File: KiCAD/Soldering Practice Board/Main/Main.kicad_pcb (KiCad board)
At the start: 2 copper layers, 7 parts, among them U1 STM32C071R8Tx, U2 BMI160, U3 LSM6DS3

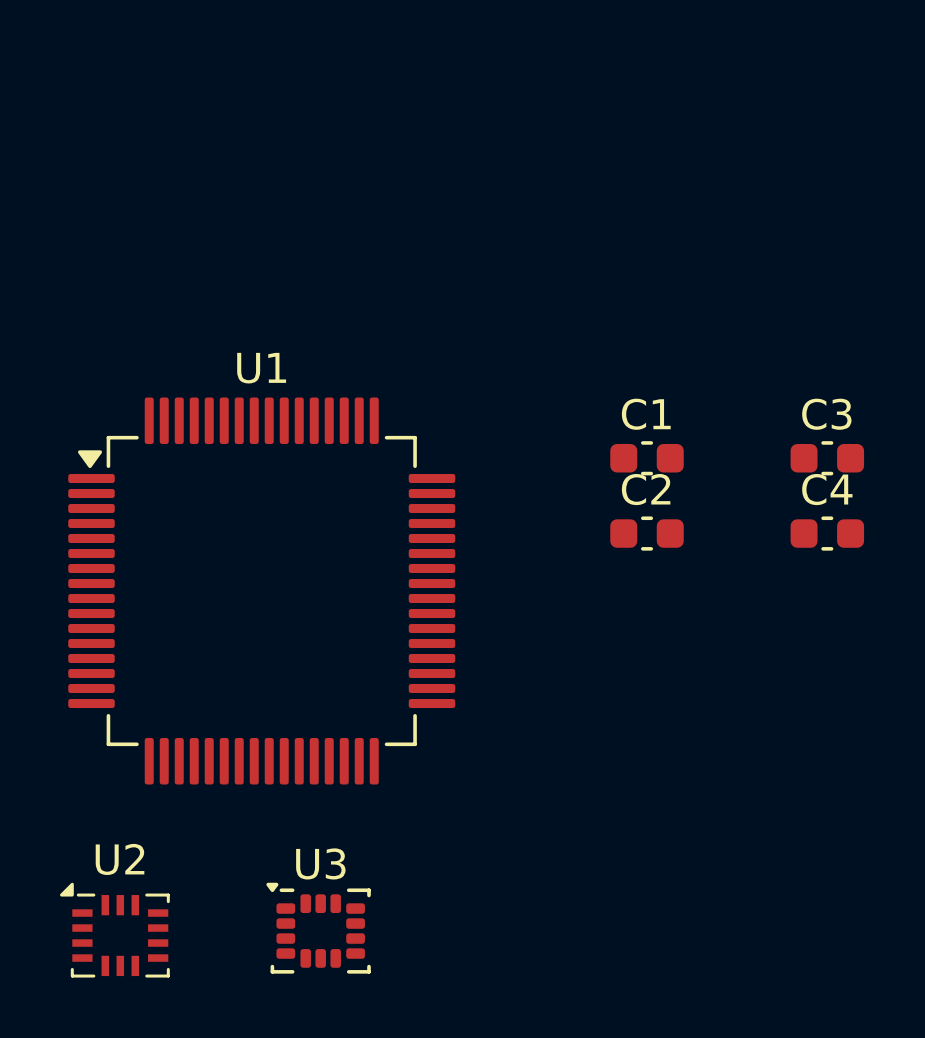
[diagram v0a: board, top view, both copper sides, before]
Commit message: Define more mcu pins
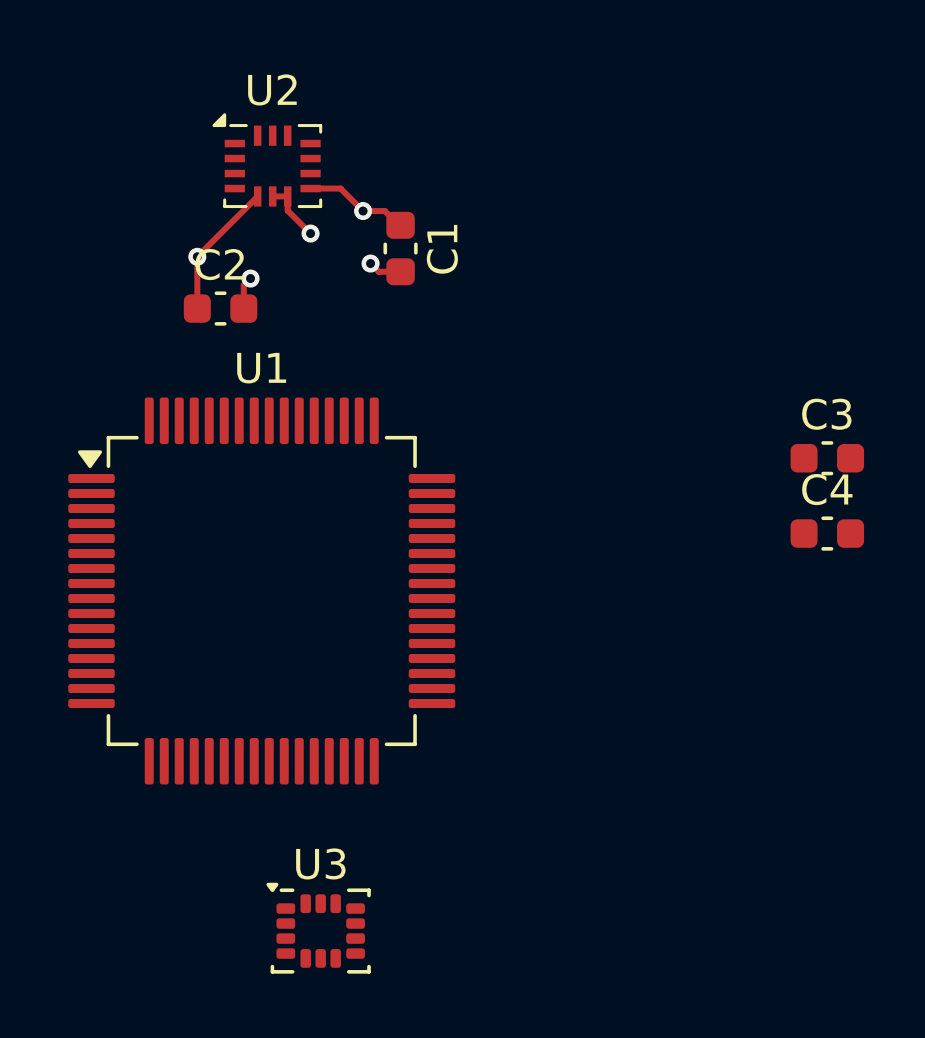
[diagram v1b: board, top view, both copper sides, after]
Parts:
- moved U2 26.1 mm to (141.7, 74.2)
- moved C2 16.1 mm to (140.0, 79.0)
- moved C1 10.8 mm to (146.0, 77.0), turned to -90 degrees
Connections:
- U1 pad 16: unconnected-(U1-PC3-Pad16) -> /TIM2_CH3
- U1 pad 25: unconnected-(U1-PC4-Pad25) -> /USART1_TX
- U1 pad 26: unconnected-(U1-PC5-Pad26) -> /USART1_RX
- U1 pad 36: unconnected-(U1-PA8-Pad36) -> /TIM1_CH1
- U1 pad 45: unconnected-(U1-PA13-Pad45) -> /SWDIO
- U1 pad 46: unconnected-(U1-PA14-Pad46) -> /SWCLK
- U1 pad 53: unconnected-(U1-PD3-Pad53) -> /STLIS_CS
- U1 pad 54: unconnected-(U1-PD4-Pad54) -> /BMI_CS
- U1 pad 55: unconnected-(U1-PD5-Pad55) -> /SPI1_MISO
- U1 pad 56: unconnected-(U1-PD6-Pad56) -> /SPI1_MOSI
- U1 pad 57: unconnected-(U1-PB3-Pad57) -> /SPI1_SCK
- U1 pad 60: unconnected-(U1-PB6-Pad60) -> /I2C1_SCL
- U1 pad 61: unconnected-(U1-PB7-Pad61) -> /I2C1_SDA
- U1 pad 7: unconnected-(U1-VREF+-Pad7) -> +3V3
- U1 pad 8: unconnected-(U1-VDD-Pad8) -> +3V3
- U1 pad 9: unconnected-(U1-VSS-Pad9) -> GND
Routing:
- net +3V3: track 0.00 -> 7.71 mm, vias 0 -> 2
- net GND: track 0.00 -> 4.26 mm, vias 0 -> 3
